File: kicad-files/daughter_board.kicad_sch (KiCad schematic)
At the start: 19 parts, among them J1 TYPE-C-31-M-12, T1 53261-0471, U1 TPD4E05U06DQAR, U2 MCP1700T-3302E/TT

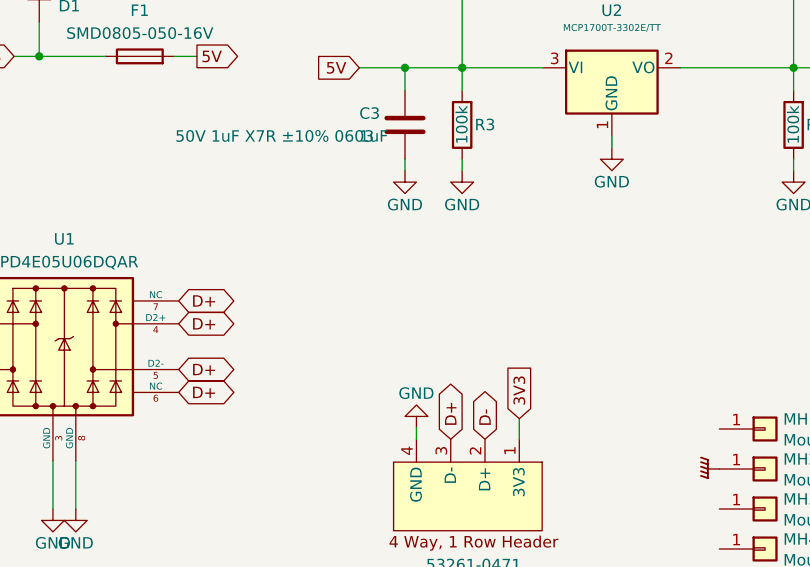
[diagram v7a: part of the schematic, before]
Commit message: Added header for 5V on daughter board and updated BOM a little
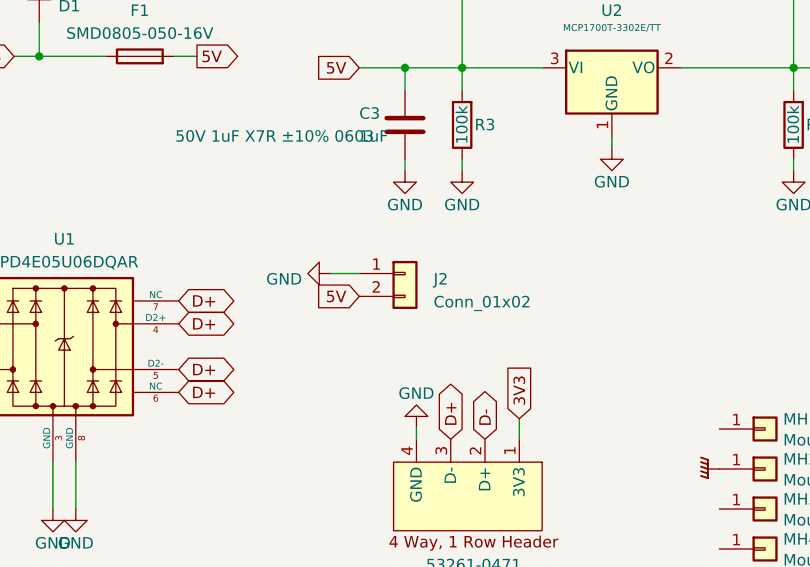
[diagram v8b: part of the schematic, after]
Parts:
- added J2: Conn_01x02, acheron_Connectors:PinHeader_1x2_P2.54mm_Vertical, symbol Connector_Generic:Conn_01x02
- C3, C5: LCSC Part C90540 -> (none); Vendor Part Number (none) -> LCSC C90540
- D1: LCSC Part Number C502546 -> (none); Vendor Part Number (none) -> LCSC C502546
- F1: LCSC Part Number C2833485 -> (none); Vendor Part Number (none) -> LCSC C2833485
- J1: LCSC Part Number C165948 -> (none); Vendor Part Number (none) -> LCSC C165948
- R3, R4: LCSC Part C606167 -> (none); Vendor Part Number (none) -> LCSC C606167
- U1: LCSC Part # C138714 -> (none); Vendor Part Number (none) -> LCSC C138714
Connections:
- net 5V: now also J2.2 (Pin_2)
- net GND: now also J2.1 (Pin_1)
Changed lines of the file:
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@@
+    (stroke (width 0) (type default))
+  )
+  (wire (pts (xy 193.675 102.87) (xy 196.85 102.87))
     (stroke (width 0) (type default))
   )
@@
     )
   )
+  (global_label "5V" (shape input) (at 196.85 105.41 180) (fields_autoplaced)
+    (effects (font (size 1.27 1.27)) (justify right))
+    (property "Intersheetrefs" "${INTERSHEET_REFS}" (at 191.6461 105.41 0)
+      (effects (font (size 1.27 1.27)) (justify right) hide)
+    )
+  )
   (global_label "5V" (shape input) (at 196.85 80.01 180) (fields_autoplaced)
     (effects (font (size 1.27 1.27)) (justify right))
@@
       (effects (font (size 1.27 1.27)) hide)
     )
-    (property "LCSC Part" "C606167" (at 245.11 86.36 0)
+    (property "LCSC Part" "" (at 245.11 86.36 0)
       (effects (font (size 1.27 1.27)) hide)
     )
@@
     )
     (property "Manufacturer" "YAGEO" (at 245.11 86.36 0)
+      (effects (font (size 1.27 1.27)) hide)
+    )
+    (property "Vendor Part Number" "LCSC C606167" (at 245.11 86.36 0)
       (effects (font (size 1.27 1.27)) hide)
     )
@@
       (effects (font (size 1.27 1.27)) hide)
     )
-    (property "LCSC Part Number" "C2833485" (at 172.466 78.74 90)
+    (property "LCSC Part Number" "" (at 172.466 78.74 90)
+      (effects (font (size 1.27 1.27)) hide)
+    )
+    (property "Vendor Part Number" "LCSC C2833485" (at 172.466 78.74 0)
       (effects (font (size 1.27 1.27)) hide)
     )
@@
       (effects (font (size 1.27 1.27)) hide)
     )
-    (property "LCSC Part #" "C138714" (at 164.084 91.948 0)
+    (property "LCSC Part #" "" (at 164.084 91.948 0)
       (effects (font (size 1.27 1.27)) hide)
     )
     (property "Package" "uSON-10" (at 164.084 89.408 0)
+      (effects (font (size 1.27 1.27)) hide)
+    )
+    (property "Vendor Part Number" "LCSC C138714" (at 164.084 110.998 0)
       (effects (font (size 1.27 1.27)) hide)
     )
@@
     )
   )
+  (symbol (lib_id "power:GND") (at 193.675 102.87 270) (unit 1)
+    (in_bom yes) (on_board yes) (dnp no) (fields_autoplaced)
+    (property "Reference" "#PWR032" (at 187.325 102.87 0)
+      (effects (font (size 1.27 1.27)) hide)
+    )
+    (property "Value" "GND" (at 190.5 103.505 90)
+      (effects (font (size 1.27 1.27)) (justify right))
+    )
+    (property "Footprint" "" (at 193.675 102.87 0)
+      (effects (font (size 1.27 1.27)) hide)
+    )
+    (property "Datasheet" "" (at 193.675 102.87 0)
+      (effects (font (size 1.27 1.27)) hide)
+    )
+    (pin "1")
+    (instances
+      (project "old_layout"
+        (path "/2fda2561-53ed-4930-8b41-858e0e3dd5f4"
+          (reference "#PWR032") (unit 1)
+        )
+      )
+      (project "daughter_board"
+        (path "/5fbc77d5-0b17-4c7b-9496-7422d8d21889"
+          (reference "#PWR07") (unit 1)
+        )
+      )
+    )
+  )
   (symbol (lib_id "Device:R") (at 208.28 86.36 180) (unit 1)
     (in_bom yes) (on_board yes) (dnp no)
@@
       (effects (font (size 1.27 1.27)) hide)
     )
-    (property "LCSC Part" "C606167" (at 208.28 86.36 0)
+    (property "LCSC Part" "" (at 208.28 86.36 0)
       (effects (font (size 1.27 1.27)) hide)
     )
@@
     )
     (property "Manufacturer" "YAGEO" (at 208.28 86.36 0)
+      (effects (font (size 1.27 1.27)) hide)
+    )
+    (property "Vendor Part Number" "LCSC C606167" (at 208.28 86.36 0)
       (effects (font (size 1.27 1.27)) hide)
     )
@@
     )
   )
+  (symbol (lib_id "Connector_Generic:Conn_01x02") (at 201.93 102.87 0) (unit 1)
+    (in_bom yes) (on_board yes) (dnp no) (fields_autoplaced)
+    (property "Reference" "J2" (at 205.105 103.505 0)
+      (effects (font (size 1.27 1.27)) (justify left))
+    )
+    (property "Value" "Conn_01x02" (at 205.105 106.045 0)
+      (effects (font (size 1.27 1.27)) (justify left))
+    )
+    (property "Footprint" "acheron_Connectors:PinHeader_1x2_P2.54mm_Vertical" (at 201.93 102.87 0)
+      (effects (font (size 1.27 1.27)) hide)
+    )
+    (property "Datasheet" "~" (at 201.93 102.87 0)
+      (effects (font (size 1.27 1.27)) hide)
+    )
+    (pin "1")
+    (pin "2")
+    (instances
+      (project "daughter_board"
+        (path "/5fbc77d5-0b17-4c7b-9496-7422d8d21889"
+          (reference "J2") (unit 1)
+        )
+      )
+    )
+  )
   (symbol (lib_id "Device:D_Schottky") (at 224.79 69.85 0) (unit 1)
     (in_bom yes) (on_board yes) (dnp no) (fields_autoplaced)
@@
       (effects (font (size 1.27 1.27)) hide)
     )
-    (property "LCSC Part" "C90540" (at 255.27 86.36 0)
+    (property "LCSC Part" "" (at 255.27 86.36 0)
       (effects (font (size 1.27 1.27)) hide)
     )
@@
     )
     (property "Manufacturer" "Guangdong Fenghua Advanced Tech" (at 255.27 86.36 0)
+      (effects (font (size 1.27 1.27)) hide)
+    )
+    (property "Vendor Part Number" "LCSC C90540" (at 255.27 86.36 0)
       (effects (font (size 1.27 1.27)) hide)
     )
@@
       (effects (font (size 1.27 1.27)) hide)
     )
-    (property "LCSC Part" "C90540" (at 201.93 86.36 0)
+    (property "LCSC Part" "" (at 201.93 86.36 0)
       (effects (font (size 1.27 1.27)) hide)
     )
@@
     )
     (property "Manufacturer" "Guangdong Fenghua Advanced Tech" (at 201.93 86.36 0)
+      (effects (font (size 1.27 1.27)) hide)
+    )
+    (property "Vendor Part Number" "LCSC C90540" (at 201.93 86.36 0)
       (effects (font (size 1.27 1.27)) hide)
     )
@@
       (effects (font (size 1.27 1.27)) hide)
     )
-    (property "LCSC Part Number" "C165948" (at 115.062 105.41 0)
+    (property "LCSC Part Number" "" (at 115.062 105.41 0)
       (effects (font (size 1.27 1.27)) hide)
     )
     (property "Manufacturer" "Koren Hroparts" (at 115.062 105.41 0)
+      (effects (font (size 1.27 1.27)) hide)
+    )
+    (property "Vendor Part Number" "LCSC C165948" (at 115.062 105.41 0)
       (effects (font (size 1.27 1.27)) hide)
     )
@@
       (effects (font (size 1.27 1.27)) hide)
     )
-    (property "LCSC Part Number" "C502546" (at 161.29 71.12 0)
+    (property "LCSC Part Number" "" (at 161.29 71.12 0)
       (effects (font (size 1.27 1.27)) hide)
     )
@@
       (effects (font (size 1.27 1.27)) hide)
     )
+    (property "Vendor Part Number" "LCSC C502546" (at 161.29 71.12 0)
+      (effects (font (size 1.27 1.27)) hide)
+    )
